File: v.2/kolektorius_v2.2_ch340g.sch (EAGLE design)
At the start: 86 parts, among them IC1 LM1117-33, IC2 ENC28J60, K2 G5V1, K3 JRC-21F(4100), T1 2N2222, T3 2N2222, T4 2N2222, U1 ATMEGA328P, X1 32.768kHz, X10 22-23-2031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

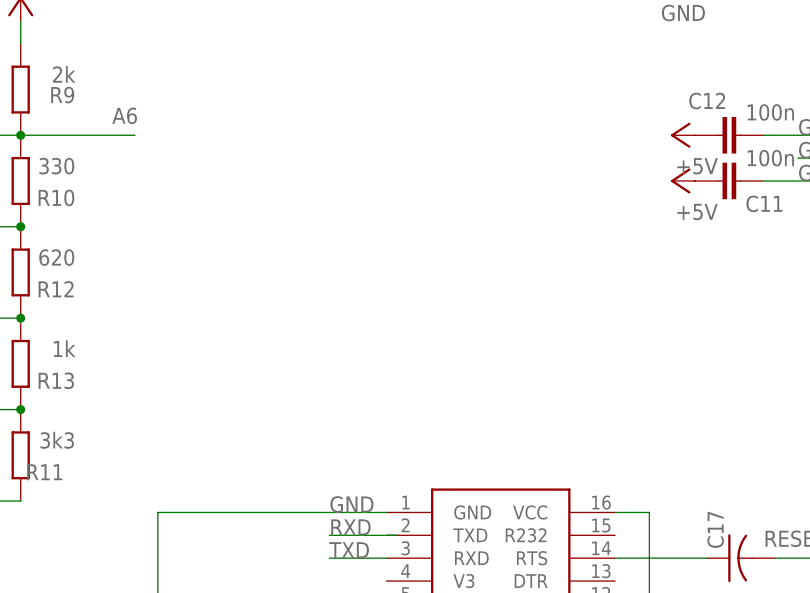
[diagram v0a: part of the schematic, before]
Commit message: pridėtas  švilpukas
išnaudoti visi kontaktai
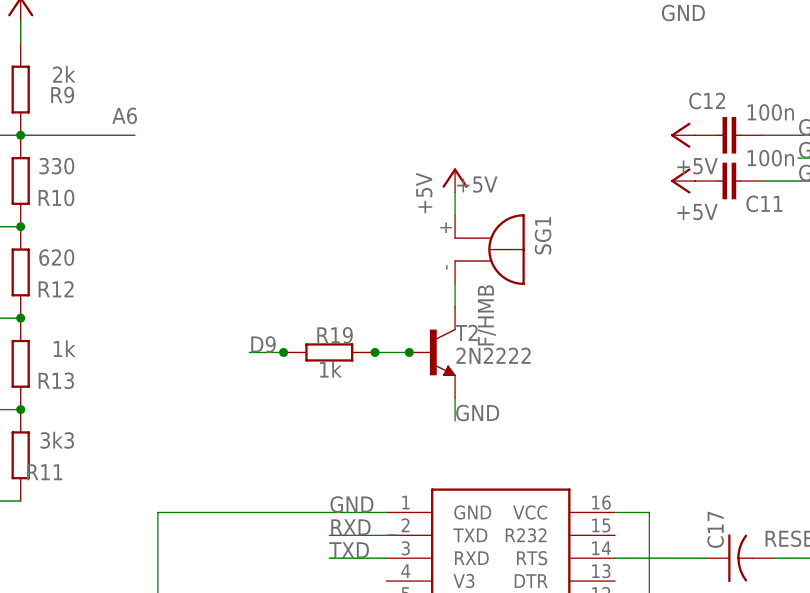
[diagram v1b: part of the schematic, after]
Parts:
- added R19: 1k, rcl:R-EU_R0805
- added SG1: F/HMB, buzzer:F/HMB
- added T2: 2N2222, adafruit:2N2222
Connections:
- new net N$27: R19.1, T2.B
- new net N$29: SG1.-, T2.C
- net +5V: now also SG1.+
- net D9: now also R19.2
- net GND: now also T2.E
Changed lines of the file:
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@@
 <part name="SJ2" library="rcl" deviceset="R-EU_" device="R0402" value="0R"/>
 <part name="SJ3" library="rcl" deviceset="R-EU_" device="R0402" value="0R"/>
+<part name="SG1" library="buzzer" deviceset="F/HMB" device=""/>
+<part name="T2" library="adafruit" deviceset="2N2222" device=""/>
+<part name="R19" library="rcl" deviceset="R-EU_" device="R0805" value="1k"/>
+<part name="+3V9" library="supply1" deviceset="+5V" device=""/>
 </parts>
 <sheets>
@@
 <instance part="SJ2" gate="G$1" x="304.8" y="73.66"/>
 <instance part="SJ3" gate="G$1" x="304.8" y="57.15"/>
+<instance part="SG1" gate="G$1" x="121.92" y="50.8" rot="R270"/>
+<instance part="T2" gate="G$1" x="116.84" y="38.1" smashed="yes">
+<attribute name="NAME" x="119.38" y="39.37" size="1.778" layer="95"/>
+<attribute name="VALUE" x="119.38" y="36.83" size="1.778" layer="96"/>
+</instance>
+<instance part="R19" gate="G$1" x="105.41" y="38.1" smashed="yes" rot="R180">
+<attribute name="NAME" x="103.8606" y="39.116" size="1.778" layer="95"/>
+<attribute name="VALUE" x="104.14" y="35.306" size="1.778" layer="96"/>
+</instance>
+<instance part="+3V9" gate="1" x="119.38" y="58.42"/>
 </instances>
 <busses>
@@
 <junction x="114.3" y="-7.62"/>
 </segment>
+<segment>
+<pinref part="T2" gate="G$1" pin="E"/>
+<wire x1="119.38" y1="33.02" x2="119.38" y2="30.48" width="0.1524" layer="91"/>
+<label x="119.38" y="30.48" size="1.778" layer="95"/>
+</segment>
 </net>
 <net name="RESET" class="0">
@@
 <wire x1="210.82" y1="64.77" x2="215.9" y2="64.77" width="0.1524" layer="91"/>
 <label x="213.36" y="64.77" size="1.778" layer="95"/>
+</segment>
+<segment>
+<wire x1="100.33" y1="38.1" x2="96.52" y2="38.1" width="0.1524" layer="91"/>
+<label x="96.52" y="38.1" size="1.778" layer="95"/>
+<pinref part="R19" gate="G$1" pin="2"/>
+<junction x="100.33" y="38.1"/>
 </segment>
 </net>
@@
 <junction x="106.68" y="-17.78"/>
 </segment>
+<segment>
+<pinref part="SG1" gate="G$1" pin="+"/>
+<wire x1="119.38" y1="53.34" x2="119.38" y2="55.88" width="0.1524" layer="91"/>
+<label x="119.38" y="55.88" size="1.778" layer="95"/>
+<pinref part="+3V9" gate="1" pin="+5V"/>
+</segment>
 </net>
 <net name="N$10" class="0">
@@
 </segment>
 </net>
+<net name="N$27" class="0">
+<segment>
+<pinref part="T2" gate="G$1" pin="B"/>
+<wire x1="110.49" y1="38.1" x2="114.3" y2="38.1" width="0.1524" layer="91"/>
+<pinref part="R19" gate="G$1" pin="1"/>
+<junction x="110.49" y="38.1"/>
+<junction x="114.3" y="38.1"/>
+</segment>
+</net>
+<net name="N$29" class="0">
+<segment>
+<pinref part="T2" gate="G$1" pin="C"/>
+<pinref part="SG1" gate="G$1" pin="-"/>
+<wire x1="119.38" y1="43.18" x2="119.38" y2="45.72" width="0.1524" layer="91"/>
+</segment>
+</net>
